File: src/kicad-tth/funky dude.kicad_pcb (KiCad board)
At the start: 2 copper layers, 44.2 x 25.1 mm, 25 parts, among them P1 CONN_2, P2 CONN_2, P3 CONN_2, U1 TLC2262

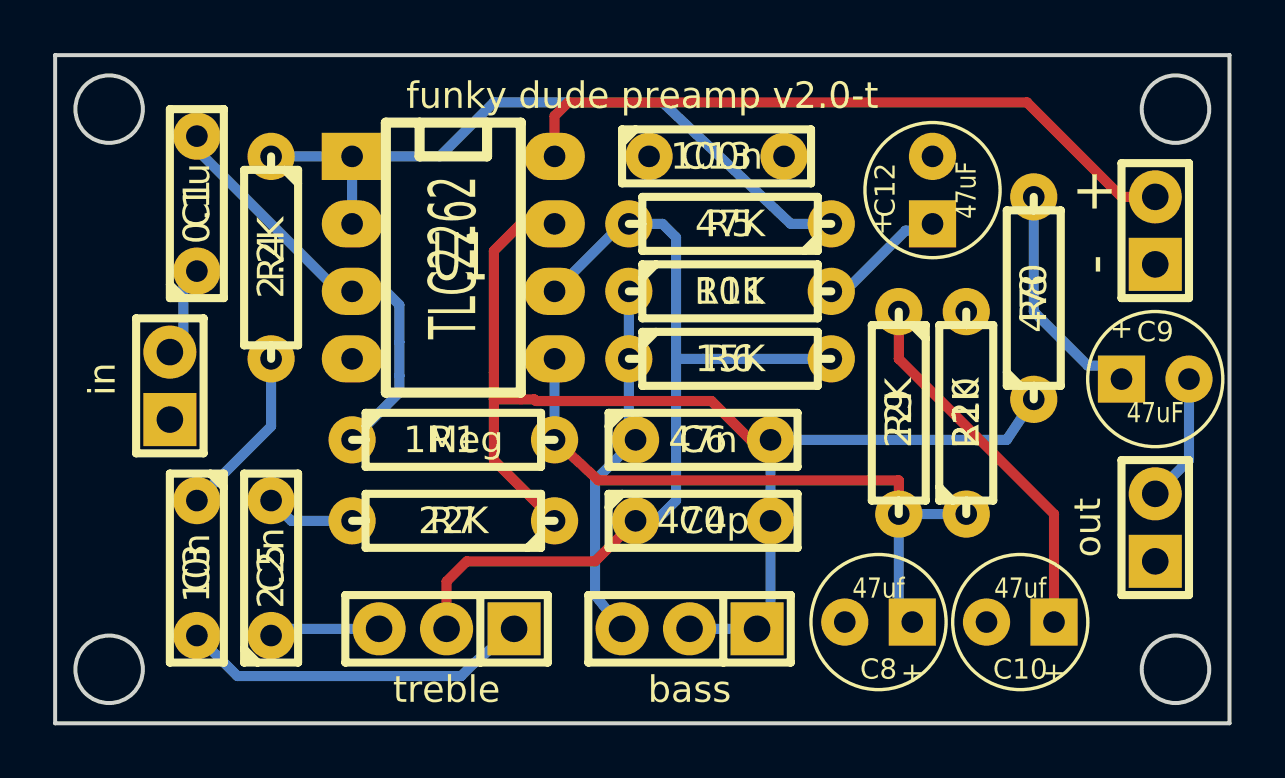
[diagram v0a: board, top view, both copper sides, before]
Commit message: adding pull-down resistors
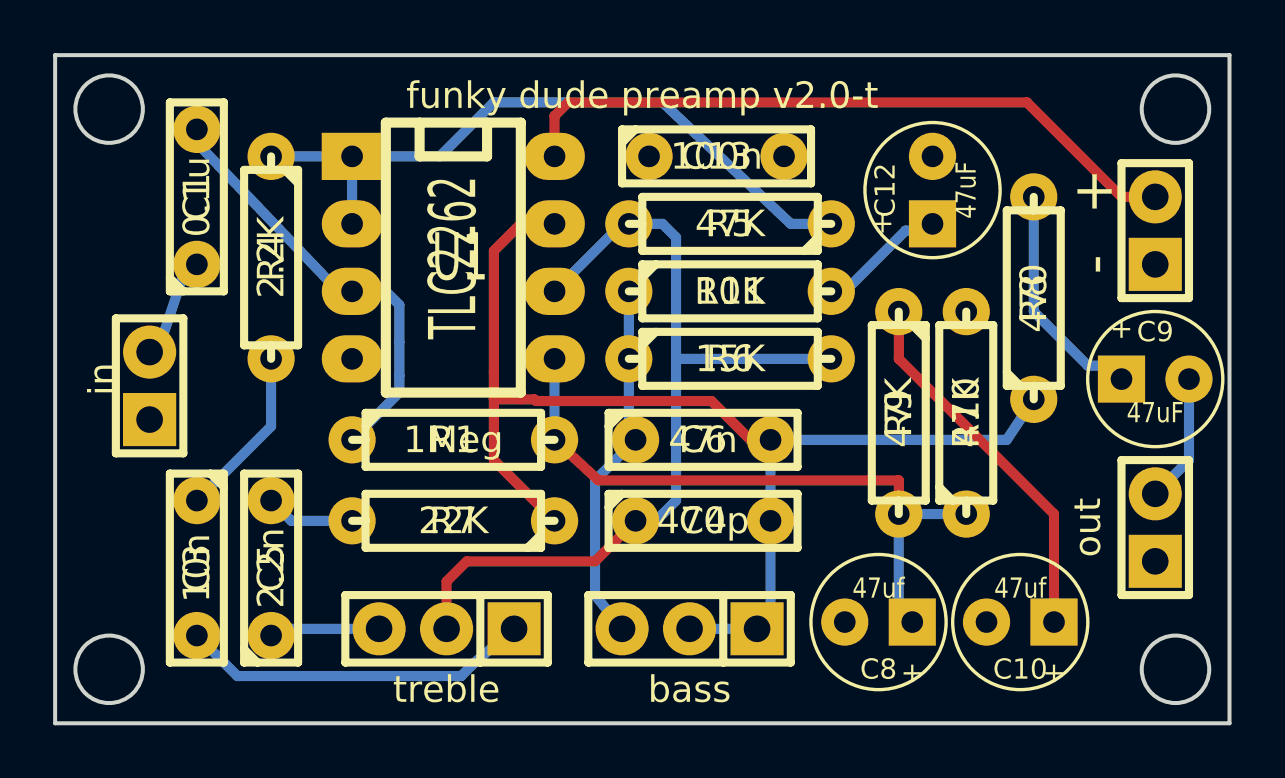
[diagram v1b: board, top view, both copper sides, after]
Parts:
- R10, R9: value 22K -> 47K
- moved P1 0.76 mm to (145.9, 118.0)
- moved C1 0.25 mm to (147.7, 110.9)

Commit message: pull-down R deleted, new plot files
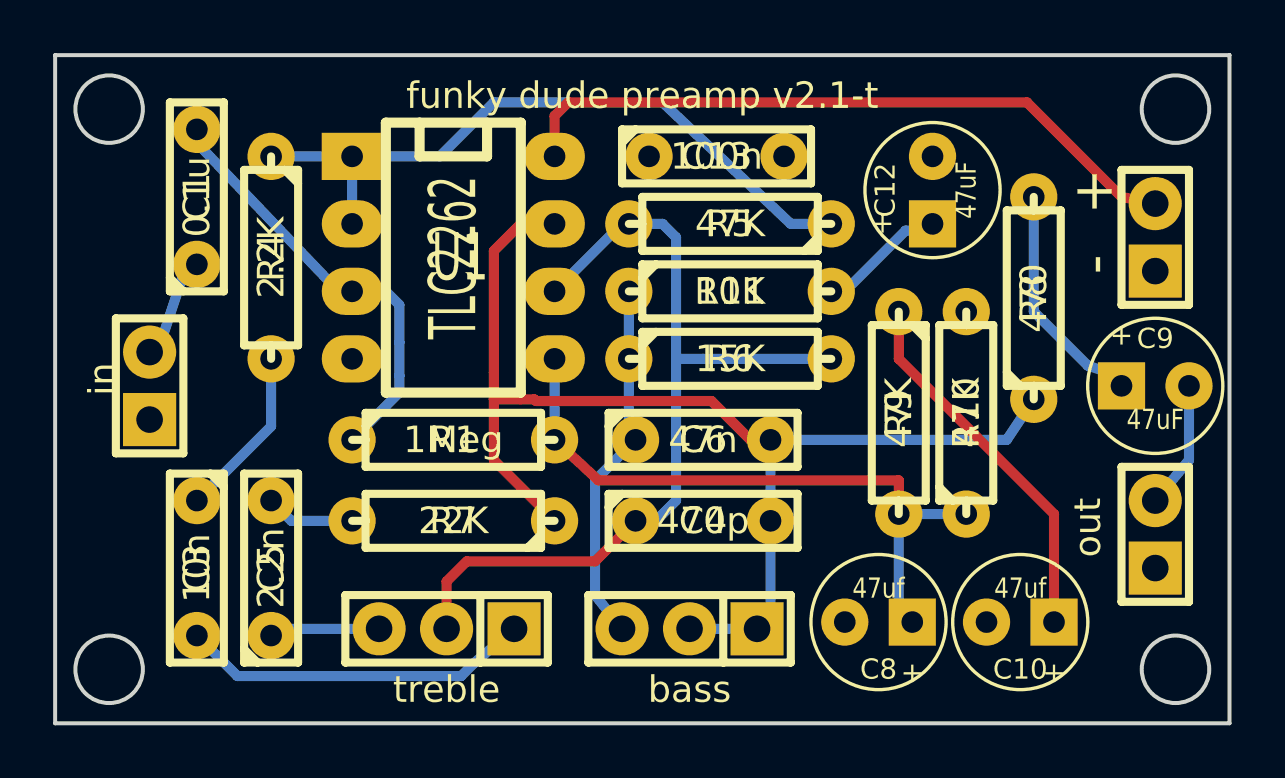
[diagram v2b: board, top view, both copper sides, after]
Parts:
- moved C9 0.25 mm to (183.8, 118.0)
- moved P2 0.25 mm to (183.8, 123.6)
- moved P3 0.25 mm to (183.8, 112.4)
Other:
- board text added: "funky dude preamp v2.1-t"
- board text removed: "funky dude preamp v2.0-t"
